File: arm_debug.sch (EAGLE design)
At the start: 11 parts

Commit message: Saving place.. currently working on Rev B
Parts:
- removed DEBUG: (no value), pinhead:PINHD-1X6
- removed LED2: (no value), led:LEDSML0805
- removed TP_5V, TP_GND0, TP_GND1, TP_VCC: 1625854-3, 1625854-3:1625854-3
- added C1, C2: (no value), resistor:C-EUC0805
- added IC1: FT230XSS, FT230XS:FT230XSS
- added JP1, JP2, PWR_SELECT: (no value), pinhead:PINHD-1X3
- added P1: 0473460001, 0473460001:0473460001
- added R2, R3, R4, R6, R7: (no value), resistor:R-US_R0805
- added TP1, TP2, TP4: TPTP20SQ, testpad:TPTP20SQ
- added U1: CAT6219, CAT6219-330TDGT3:CAT6219
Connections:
- removed net !CTS: DEBUG.2
- removed net !RTS: DEBUG.6
- removed net VCC: DEVICE.1, PROG.1, R1.2, TP_VCC.1, TP_VCC.2
- new net +3V3: PWR_SELECT.3, TP2.TP, U1.VOUT
- new net D+: C2.1, IC1.USBDP, R7.1
- new net D-: C1.1, IC1.USBDM, R1.1
- new net FT230_RX: IC1.RXD, JP1.2
- new net FT230_TX: IC1.TXD, JP2.2
- new net N$3: IC1.!RESET, IC1.3V3OUT, IC1.VCCIO
- new net N$4: P1.D+, R7.2
- new net N$7: JP2.3, R4.1, R6.2
- new net N$8: JP1.3, R2.2, R3.1
- new net TARGET_PWR: DEVICE.1, PROG.1, PWR_SELECT.2
- net +5V: now also IC1.VCC, P1.VBUS, PWR_SELECT.1, TP1.TP, U1.EN, U1.VIN; no longer DEBUG.3, TP_5V.1, TP_5V.2
- net DEBUG_UART_RX: now also JP2.1, R4.2; no longer DEBUG.4
- net DEBUG_UART_TX: now also JP1.1, R3.2; no longer DEBUG.5
- net GND: now also C1.2, C2.2, IC1.GND, IC1.GND@1, P1.GND, R2.1, R6.1, TP4.TP, U1.GND; no longer DEBUG.1, LED2.C, TP_GND0.1, TP_GND0.2, TP_GND1.1, TP_GND1.2
- net N$2: now also P1.D-, R1.2; no longer LED2.A, R1.1
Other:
- note removed: "CTS# / BROWN"
- note removed: "GND / BLACK"
- note removed: "RTS# / GREEN"
- note removed: "RXD / YELLOW"
- note removed: "TXD / ORANGE"
- note removed: "VCC / RED"
- moved on the sheet: DEVICE, LED1, PROG, R1, R5

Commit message: Committing RevB
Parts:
- removed IC1: FT230XSS, FT230XS:FT230XSS
- removed JP1, JP2, PWR_SELECT: (no value), pinhead:PINHD-1X3
- removed R6: (no value), resistor:R-US_R0805
- removed TP1, TP2, TP4: TPTP20SQ, testpad:TPTP20SQ
- added C3: .1uF, resistor:C-EUC0603
- added LED2, LED3: (no value), led:LEDCHIPLED_0603
- added S1: 431151015826, 431151015826:431151015826
- C1, C2: value (none) -> 47pF; device resistor:C-EUC0805 -> resistor:C-EUC0603
- LED1: device led:LEDSML0805 -> led:LEDCHIPLED_0603
- R1, R4, R7: value (none) -> 27; device resistor:R-US_R0805 -> resistor:R-US_R0603
- R2, R3: value (none) -> 330; device resistor:R-US_R0805 -> resistor:R-US_R0603
- R5: value (none) -> 1K; device resistor:R-US_R0805 -> resistor:R-US_R0603
- U1: value CAT6219 -> FT230XQ-T; device CAT6219-330TDGT3:CAT6219 -> FT230XQ-T:FT230XQ-T
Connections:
- removed net +3V3: PWR_SELECT.3, TP2.TP, U1.VOUT
- removed net FT230_RX: IC1.RXD, JP1.2
- removed net FT230_TX: IC1.TXD, JP2.2
- removed net N$1: LED1.A, R5.1
- removed net N$7: JP2.3, R4.1, R6.2
- removed net N$8: JP1.3, R2.2, R3.1
- new net N$14: LED1.A, R2.1
- new net N$9: LED2.A, R3.1
- new net RXLED: LED2.C, U1.CBUS2
- new net TXLED: LED1.C, U1.CBUS1
- new net VCCIO: C3.1, R2.2, R3.2, U1.!RESET!, U1.3V3OUT, U1.VCCIO
- net !RESET: now also R5.1, S1.2
- net +5V: now also R4.2, U1.VCC; no longer IC1.VCC, PWR_SELECT.1, R5.2, TP1.TP, U1.EN, U1.VIN
- net D+: now also U1.USBDP; no longer IC1.USBDP
- net D-: now also U1.USBDM; no longer IC1.USBDM
- net DEBUG_UART_RX: now also U1.TXD; no longer JP2.1, R4.2
- net DEBUG_UART_TX: now also U1.RXD; no longer JP1.1, R3.2
- net GND: now also C3.2, LED3.C, S1.1, S1.5, S1.6, U1.GND@13, U1.GND@17, U1.GND@3; no longer IC1.GND, IC1.GND@1, LED1.C, R2.1, R6.1, TP4.TP, U1.GND
- net N$3: now also LED3.A, R4.1; no longer IC1.!RESET, IC1.3V3OUT, IC1.VCCIO
- net TARGET_PWR: now also R5.2; no longer PWR_SELECT.2
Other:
- note removed: "Debug"
- note removed: "Power LED"
- note removed: "Test Pads"
- moved on the sheet: C1, C2, DEVICE, LED1, P1, PROG, R1, R2, R3, R4, R5, R7

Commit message: Commiting RevC
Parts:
- removed DEVICE, PROG: FTSH-105-01-L-DV-K, FTSH-105-01-L-DV-K:FTSH-105-01-L-DV-K
- added P2: CORTEX-SWD, programming_headers:SWD-CORTEX
- added P3: MOLEX_MICRO_USB, board_connectivity:MOLEX_MICRO_USB
- P1: value 0473460001 -> CORTEX-SWD; device 0473460001:0473460001 -> programming_headers:SWD-CORTEX
- R4: value 27 -> 330
- S1: value 431151015826 -> WURTH_SMD_PB; device 431151015826:431151015826 -> switches:WURTH_SMD_PB
- U1: value FT230XQ-T -> FT230X; device FT230XQ-T:FT230XQ-T -> USB:FT230XQ
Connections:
- removed net N/C: PROG.6, PROG.8
- net !RESET: now also P1.10, P2.10; no longer DEVICE.10, PROG.10
- net +5V: now also P3.VBUS; no longer P1.VBUS
- net DEBUG_UART_RX: now also P2.7; no longer DEVICE.6
- net DEBUG_UART_TX: now also P2.9; no longer DEVICE.8
- net GND: now also P1.3, P1.5, P1.7, P1.9, P2.3, P2.5, P3.GND, U1.GND; no longer DEVICE.3, DEVICE.5, DEVICE.7, DEVICE.9, P1.GND, PROG.3, PROG.5, PROG.7, PROG.9, U1.GND@13, U1.GND@17, U1.GND@3
- net N$2: now also P3.D-; no longer P1.D-
- net N$4: now also P3.D+; no longer P1.D+
- net RXLED: now also U1.CBUS1; no longer U1.CBUS2
- net SWDCLK: now also P1.4, P2.4; no longer DEVICE.4, PROG.4
- net SWDIO: now also P1.2, P2.2; no longer DEVICE.2, PROG.2
- net TARGET_PWR: now also P1.1, P2.1; no longer DEVICE.1, PROG.1
- net TXLED: now also U1.CBUS0; no longer U1.CBUS1
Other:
- note added: "FT230X UART to USB Bridge"
- note added: "Micro USB Connector"
- note added: "Reset Pushbutton"
- note added: "User Indicators"
- moved on the sheet: C1, C2, C3, LED1, LED2, LED3, R1, R2, R3, R4, R5, R7

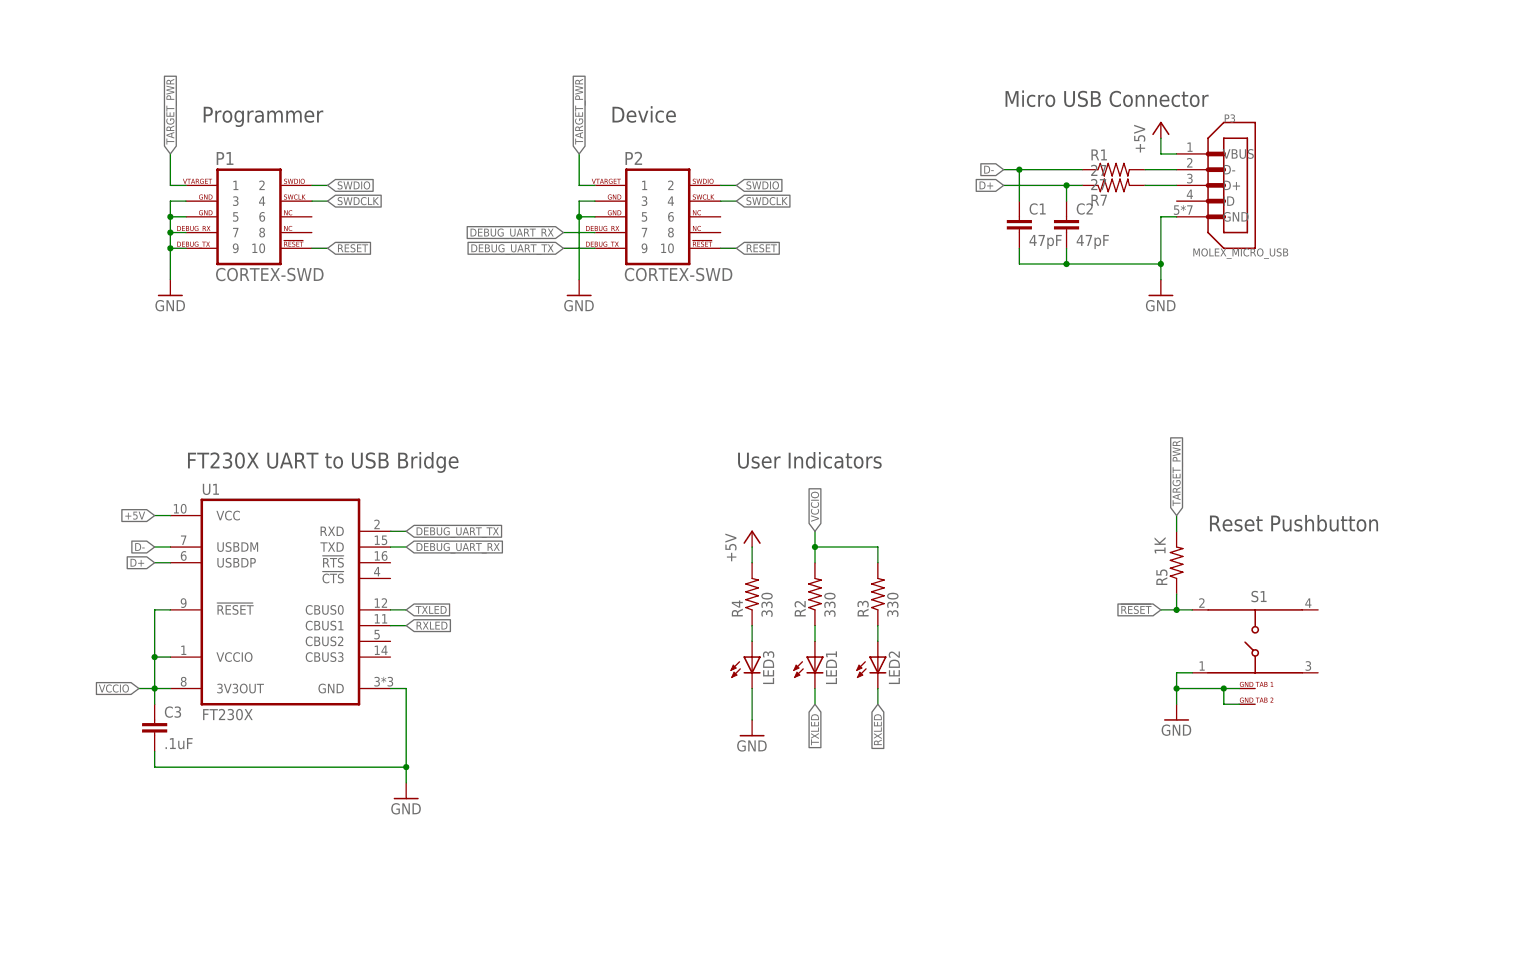
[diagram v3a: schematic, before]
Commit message: Adding MEC connector for edge card connectors
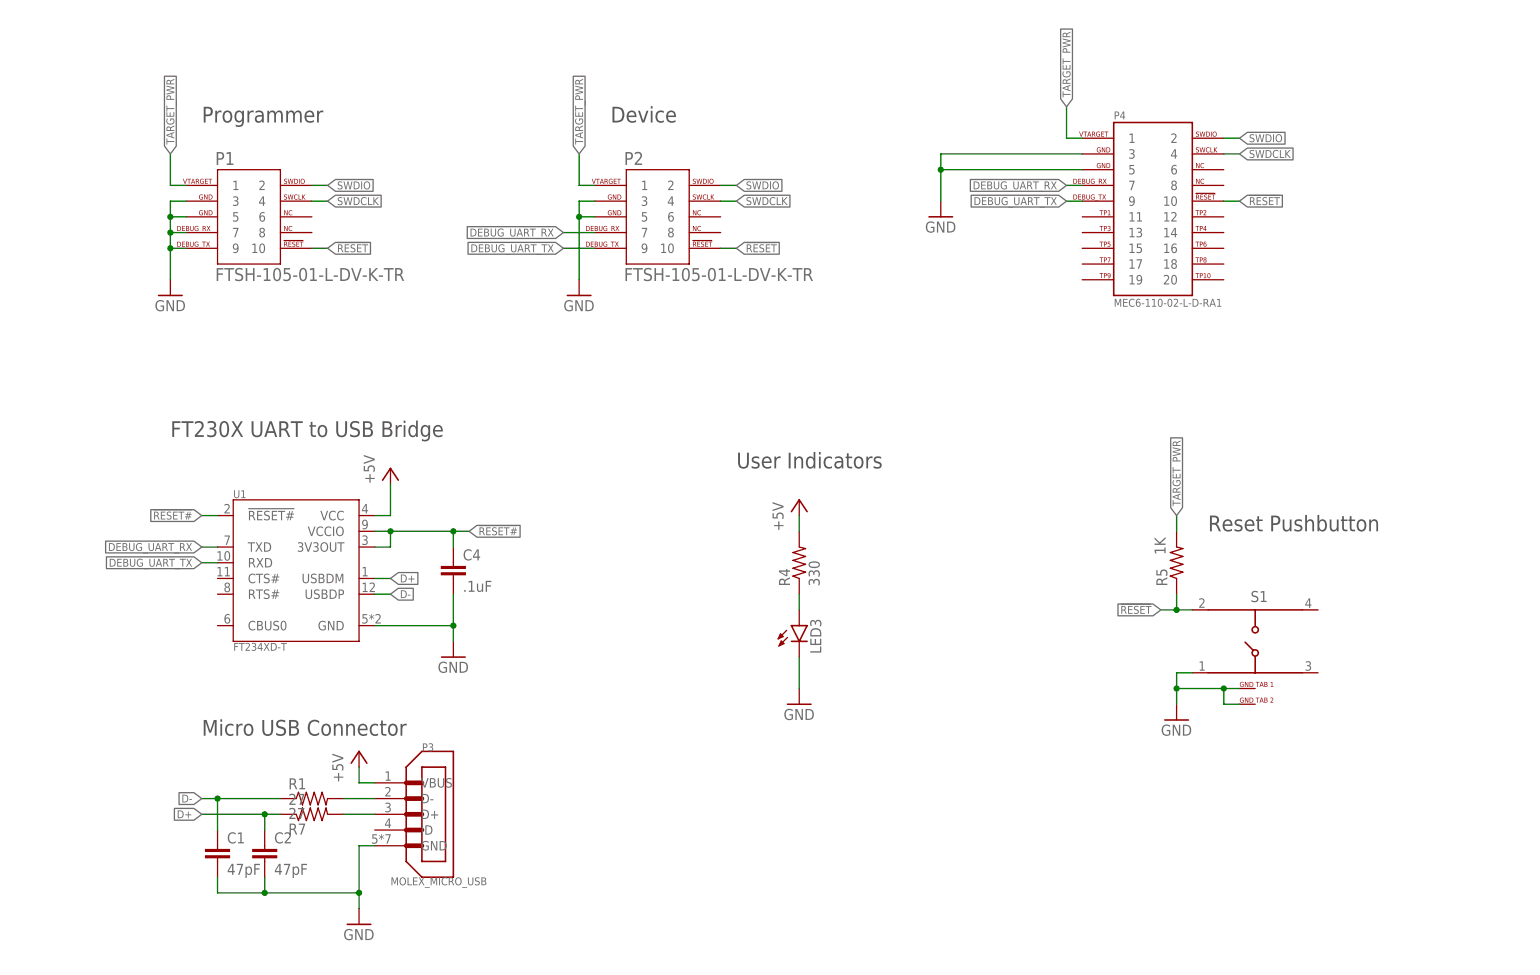
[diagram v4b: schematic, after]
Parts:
- removed C3: .1uF, resistor:C-EUC0603
- removed LED1, LED2: (no value), led:LEDCHIPLED_0603
- removed R2, R3: 330, resistor:R-US_R0603
- added C4: .1uF, resistor:C-EUC0603
- added P4: MEC6-110-02-L-D-RA1, programming_headers:SWD-MEC10-F
- P1, P2: value CORTEX-SWD -> FTSH-105-01-L-DV-K-TR
- U1: value FT230X -> FT234XD-T; device USB:FT230XQ -> USB:FT234XD-T
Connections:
- removed net N$14: LED1.A, R2.1
- removed net N$9: LED2.A, R3.1
- removed net RXLED: LED2.C, U1.CBUS1
- removed net TXLED: LED1.C, U1.CBUS0
- removed net VCCIO: C3.1, R2.2, R3.2, U1.!RESET!, U1.3V3OUT, U1.VCCIO
- new net !RESET#: C4.1, U1.!RESET#, U1.3V3OUT, U1.VCCIO
- net !RESET: now also P4.10
- net D+: now also U1.USBDM; no longer U1.USBDP
- net D-: now also U1.USBDP; no longer U1.USBDM
- net DEBUG_UART_RX: now also P4.7
- net DEBUG_UART_TX: now also P4.9
- net GND: now also C4.2, P4.3, P4.5; no longer C3.2
- net SWDCLK: now also P4.4
- net SWDIO: now also P4.2
- net TARGET_PWR: now also P4.1
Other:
- moved on the sheet: C1, C2, P3, R1, R4, R7

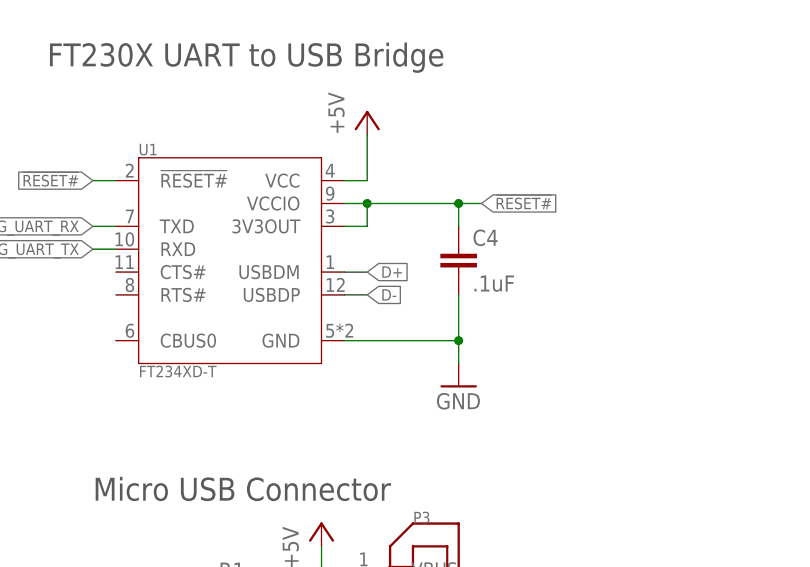
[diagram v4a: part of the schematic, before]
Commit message: Fixing issue with reversed USB Data plus and minus pins
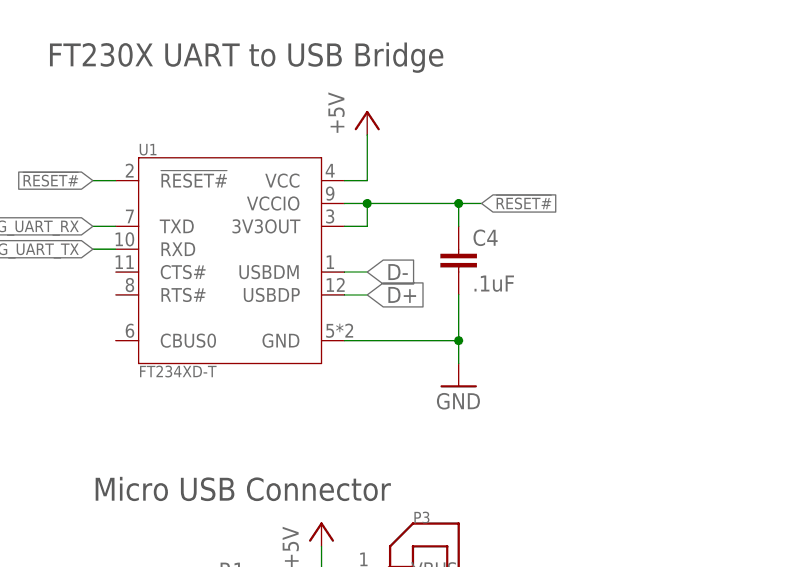
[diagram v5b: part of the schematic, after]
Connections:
- net D+: now also U1.USBDP; no longer U1.USBDM
- net D-: now also U1.USBDM; no longer U1.USBDP
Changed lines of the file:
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@@
 <?xml version="1.0" encoding="utf-8"?>
 <!DOCTYPE eagle SYSTEM "eagle.dtd">
-<eagle version="9.3.2">
+<eagle version="9.5.1">
 <drawing>
 <settings>
@@
 </segment>
 <segment>
-<pinref part="U1" gate="G$1" pin="USBDP"/>
-<wire x1="68.58" y1="73.66" x2="71.12" y2="73.66" width="0.1524" layer="91"/>
-<label x="71.12" y="73.66" size="1.27" layer="95" xref="yes"/>
+<pinref part="U1" gate="G$1" pin="USBDM"/>
+<wire x1="68.58" y1="76.2" x2="71.12" y2="76.2" width="0.1524" layer="91"/>
+<label x="71.12" y="76.2" size="1.778" layer="95" xref="yes"/>
 </segment>
 </net>
@@
 </segment>
 <segment>
-<pinref part="U1" gate="G$1" pin="USBDM"/>
-<wire x1="68.58" y1="76.2" x2="71.12" y2="76.2" width="0.1524" layer="91"/>
-<label x="71.12" y="76.2" size="1.27" layer="95" xref="yes"/>
-</segment>
-</net>
+<pinref part="U1" gate="G$1" pin="USBDP"/>
+<wire x1="68.58" y1="73.66" x2="71.12" y2="73.66" width="0.1524" layer="91"/>
+<label x="71.12" y="73.66" size="1.778" layer="95" xref="yes"/>
+</segment>
+</net>
